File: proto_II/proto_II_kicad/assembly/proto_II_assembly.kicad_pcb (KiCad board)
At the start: 2 copper layers, 100 x 97 mm, 109 parts, among them J101 BOOT_CFG, J102 SNSR_I2C, J103 SNSR_PWR, J104 Vin, J105 RS485_A, J106 RS485_B, J107 ISO_GND, J108 Vin-5V, J109 SWD_DBG, J301 SIG_BYPASS, J302 PWR_BYPASS, SW101 RST, SW102 MODBUS_ADDR, SW103 USR_BTN, U101 STM32F103C8Tx, U201 TPS54331, U202 XC6206P332MR, U301 ADUM5241, U302 EL357N-G, U303 EL357N-G, U304 ST485EBDR, Y101 HSE, Y102 LSE

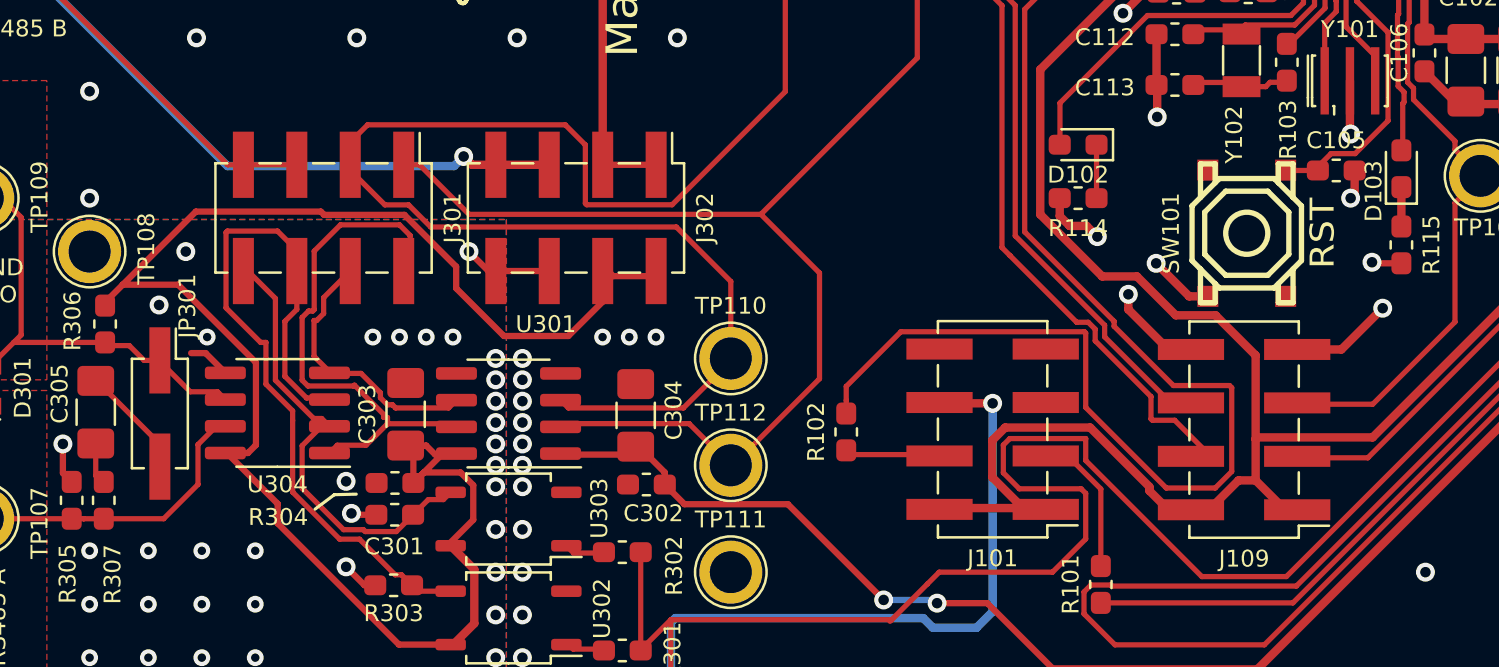
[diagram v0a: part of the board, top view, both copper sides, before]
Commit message: proto II: add more pin designators to silkscreen
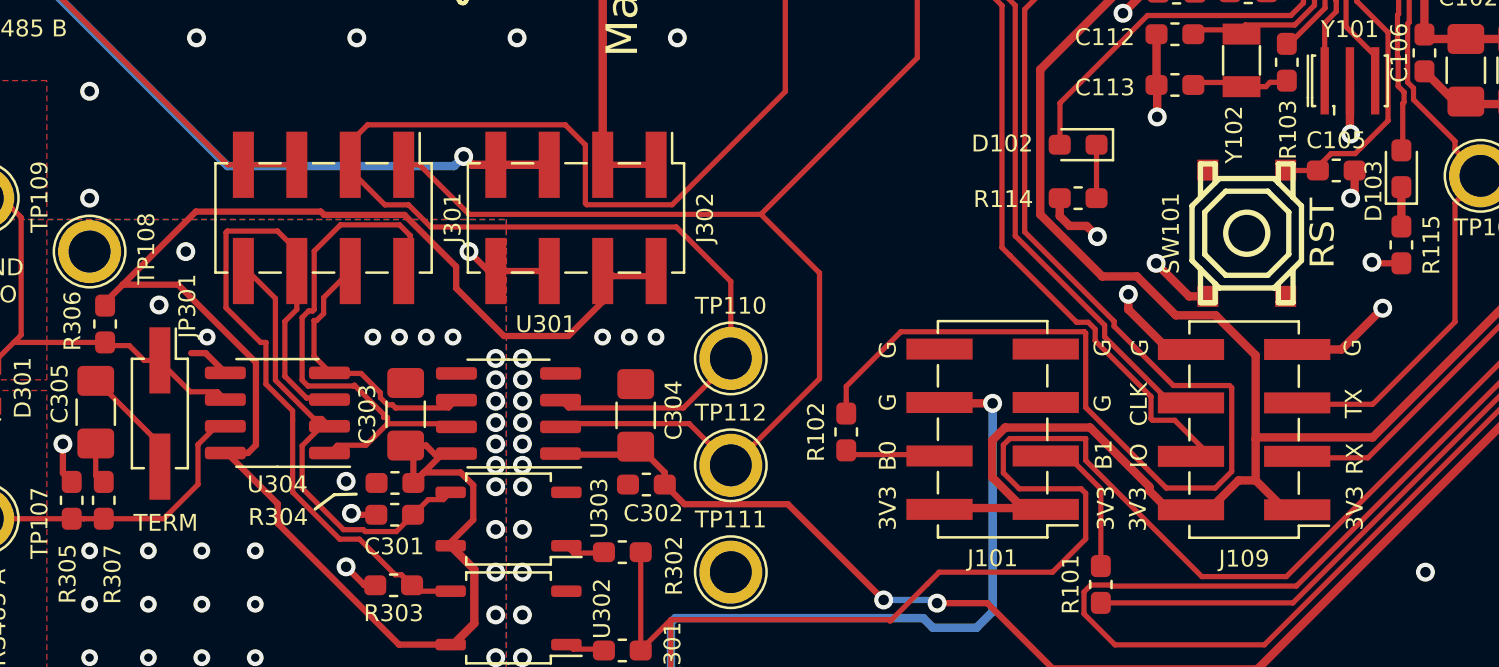
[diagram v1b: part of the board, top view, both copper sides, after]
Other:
- board text added: "3V3"
- board text added: "B0"
- board text added: "B1"
- board text added: "CLK"
- board text added: "G"
- board text added: "IO"
- board text added: "RX"
- board text added: "TERM"
- board text added: "TX"
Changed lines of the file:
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@@
   (general
     (thickness 1.6)
-    (drawings 589)
+    (drawings 606)
     (tracks 1098)
     (zones 0)
@@
   )
   (setup
-    (last_trace_width 0.4)
+    (last_trace_width 0.25)
     (user_trace_width 0.4)
     (trace_clearance 0.2)
@@
     (add_net "Net-(R301-Pad1)")
     (add_net "Net-(R302-Pad1)")
-    (add_net "Net-(U101-Pad10)")
-    (add_net "Net-(U101-Pad16)")
-    (add_net "Net-(U101-Pad18)")
-    (add_net "Net-(U101-Pad19)")
-    (add_net "Net-(U101-Pad21)")
-    (add_net "Net-(U101-Pad22)")
-    (add_net "Net-(U101-Pad25)")
-    (add_net "Net-(U101-Pad26)")
-    (add_net "Net-(U101-Pad27)")
-    (add_net "Net-(U101-Pad28)")
-    (add_net "Net-(U101-Pad45)")
-    (add_net "Net-(U101-Pad46)")
   )
   (net_class PWR ""
@@
     (tags "resistor handsolder")
     (attr smd)
-    (fp_text reference R114 (at 0 -1.43) (layer F.SilkS)
+    (fp_text reference R114 (at 3.556 -0.0508) (layer F.SilkS)
       (effects (font (size 0.8 0.8) (thickness 0.15)))
     )
@@
     (tags "diode handsolder")
     (attr smd)
-    (fp_text reference D102 (at 0 -1.43) (layer F.SilkS)
+    (fp_text reference D102 (at 3.6068 0.0508) (layer F.SilkS)
       (effects (font (size 0.8 0.8) (thickness 0.15)))
     )
@@
     )
   )
+  (gr_text IO (at 105.7656 111.3028 90) (layer F.SilkS)
+    (effects (font (size 0.8 0.8) (thickness 0.15)))
+  )
+  (gr_text CLK (at 105.7656 108.8644 90) (layer F.SilkS)
+    (effects (font (size 0.8 0.8) (thickness 0.15)))
+  )
+  (gr_text 3V3 (at 105.7148 113.8428 90) (layer F.SilkS)
+    (effects (font (size 0.8 0.8) (thickness 0.15)))
+  )
+  (gr_text 3V3 (at 116.0272 113.792 90) (layer F.SilkS)
+    (effects (font (size 0.8 0.8) (thickness 0.15)))
+  )
+  (gr_text 3V3 (at 104.1908 113.792 90) (layer F.SilkS)
+    (effects (font (size 0.8 0.8) (thickness 0.15)))
+  )
+  (gr_text RX (at 116.0272 111.4552 90) (layer F.SilkS)
+    (effects (font (size 0.8 0.8) (thickness 0.15)))
+  )
+  (gr_text TX (at 115.9764 108.8136 90) (layer F.SilkS)
+    (effects (font (size 0.8 0.8) (thickness 0.15)))
+  )
+  (gr_text G (at 115.9256 106.172 90) (layer F.SilkS)
+    (effects (font (size 0.8 0.8) (thickness 0.15)))
+  )
+  (gr_text G (at 105.8164 106.172 90) (layer F.SilkS)
+    (effects (font (size 0.8 0.8) (thickness 0.15)))
+  )
+  (gr_text G (at 104.0384 106.172 90) (layer F.SilkS)
+    (effects (font (size 0.8 0.8) (thickness 0.15)))
+  )
+  (gr_text G (at 104.0384 108.8136 90) (layer F.SilkS)
+    (effects (font (size 0.8 0.8) (thickness 0.15)))
+  )
+  (gr_text B1 (at 104.0892 111.252 90) (layer F.SilkS)
+    (effects (font (size 0.8 0.8) (thickness 0.15)))
+  )
+  (gr_text G (at 93.8276 106.2736 90) (layer F.SilkS)
+    (effects (font (size 0.8 0.8) (thickness 0.15)))
+  )
+  (gr_text G (at 93.8276 108.7628 90) (layer F.SilkS)
+    (effects (font (size 0.8 0.8) (thickness 0.15)))
+  )
+  (gr_text B0 (at 93.8276 111.3028 90) (layer F.SilkS)
+    (effects (font (size 0.8 0.8) (thickness 0.15)))
+  )
+  (gr_text 3V3 (at 93.8276 113.792 90) (layer F.SilkS)
+    (effects (font (size 0.8 0.8) (thickness 0.15)))
+  )
+  (gr_text TERM (at 59.5 114.5) (layer F.SilkS)
+    (effects (font (size 0.8 0.8) (thickness 0.15)))
+  )
   (gr_text "Proto II, rev0\n" (at 87 82 90) (layer F.SilkS)
     (effects (font (size 1.5 1.5) (thickness 0.3)))
@@
   (segment (start 121.714165 55.267767) (end 124.35607 55.267767) (width 0.4) (layer F.Cu) (net 2))
   (segment (start 112.826799 46.380401) (end 115.531999 49.085601) (width 0.4) (layer F.Cu) (net 2))
+  (segment (start 110.5408 60.9092) (end 110.5916 60.96) (width 0.4) (layer F.Cu) (net 2))
+  (segment (start 113.105469 60.730669) (end 113.1316 60.7568) (width 0.4) (layer F.Cu) (net 2))
+  (segment (start 113.336316 60.730669) (end 113.259331 60.730669) (width 0.4) (layer F.Cu) (net 2))
+  (segment (start 113.259331 60.730669) (end 113.336262 60.8076) (width 0.4) (layer F.Cu) (net 2))
+  (segment (start 121.960083 63.039917) (end 121.460083 63.039917) (width 0.4) (layer F.Cu) (net 2))
+  (segment (start 123.5 61.5) (end 121.960083 63.039917) (width 0.4) (layer F.Cu) (net 2))
+  (segment (start 121.460083 63.039917) (end 121.866317 63.039917) (width 0.4) (layer F.Cu) (net 2))
+  (segment (start 107.730669 60.730669) (end 108 61) (width 0.4) (layer F.Cu) (net 2))
+  (segment (start 108 61) (end 123.5 61) (width 0.4) (layer F.Cu) (net 2))
+  (segment (start 105.176864 63.039917) (end 121.460083 63.039917) (width 0.4) (layer F.Cu) (net 2))
+  (segment (start 123.5 61) (end 123.5 61.5) (width 0.4) (layer F.Cu) (net 2))
+  (segment (start 105.716316 60.730669) (end 107.730669 60.730669) (width 0.4) (layer F.Cu) (net 2))
+  (segment (start 121.460083 62.854436) (end 121.460083 63.039917) (width 0.4) (layer F.Cu) (net 2))
+  (segment (start 120.956316 62.350669) (end 121.460083 62.854436) (width 0.4) (layer F.Cu) (net 2))
+  (segment (start 120.956316 60.730669) (end 120.956316 62.350669) (width 0.4) (layer F.Cu) (net 2))
+  (segment (start 104.555458 60.931527) (end 103.068473 60.931527) (width 0.4) (layer F.Cu) (net 2))
+  (segment (start 105.716316 60.730669) (end 104.756316 60.730669) (width 0.4) (layer F.Cu) (net 2))
+  (segment (start 104.756316 60.730669) (end 104.555458 60.931527) (width 0.4) (layer F.Cu) (net 2))
+  (segment (start 100.560813 58.423866) (end 103.068473 60.931527) (width 0.4) (layer F.Cu) (net 2))
+  (segment (start 103.068473 60.931527) (end 105.176864 63.039917) (width 0.4) (layer F.Cu) (net 2))
   (segment (start 114.265908 97.744551) (end 112.794051 97.744551) (width 0.25) (layer F.Cu) (net 3) (status 30))
   (segment (start 112.794051 97.744551) (end 112.7125 97.663) (width 0.25) (layer F.Cu) (net 3) (status 30))
@@
   (segment (start 53.2135 71.062) (end 51.377 71.062) (width 0.4) (layer F.Cu) (net 49))
   (segment (start 51.377 71.062) (end 51.308 70.993) (width 0.4) (layer F.Cu) (net 49))
-  (segment (start 110.5408 60.9092) (end 110.5916 60.96) (width 0.4) (layer F.Cu) (net 2))
-  (segment (start 113.105469 60.730669) (end 113.1316 60.7568) (width 0.4) (layer F.Cu) (net 2))
-  (segment (start 113.336316 60.730669) (end 113.259331 60.730669) (width 0.4) (layer F.Cu) (net 2))
-  (segment (start 113.259331 60.730669) (end 113.336262 60.8076) (width 0.4) (layer F.Cu) (net 2))
-  (segment (start 121.960083 63.039917) (end 121.460083 63.039917) (width 0.4) (layer F.Cu) (net 2))
-  (segment (start 123.5 61.5) (end 121.960083 63.039917) (width 0.4) (layer F.Cu) (net 2))
-  (segment (start 121.460083 63.039917) (end 121.866317 63.039917) (width 0.4) (layer F.Cu) (net 2))
-  (segment (start 107.730669 60.730669) (end 108 61) (width 0.4) (layer F.Cu) (net 2))
-  (segment (start 108 61) (end 123.5 61) (width 0.4) (layer F.Cu) (net 2))
-  (segment (start 105.176864 63.039917) (end 121.460083 63.039917) (width 0.4) (layer F.Cu) (net 2))
-  (segment (start 123.5 61) (end 123.5 61.5) (width 0.4) (layer F.Cu) (net 2))
-  (segment (start 105.716316 60.730669) (end 107.730669 60.730669) (width 0.4) (layer F.Cu) (net 2))
-  (segment (start 121.460083 62.854436) (end 121.460083 63.039917) (width 0.4) (layer F.Cu) (net 2))
-  (segment (start 120.956316 62.350669) (end 121.460083 62.854436) (width 0.4) (layer F.Cu) (net 2))
-  (segment (start 120.956316 60.730669) (end 120.956316 62.350669) (width 0.4) (layer F.Cu) (net 2))
-  (segment (start 104.555458 60.931527) (end 103.068473 60.931527) (width 0.4) (layer F.Cu) (net 2))
-  (segment (start 105.716316 60.730669) (end 104.756316 60.730669) (width 0.4) (layer F.Cu) (net 2))
-  (segment (start 104.756316 60.730669) (end 104.555458 60.931527) (width 0.4) (layer F.Cu) (net 2))
-  (segment (start 100.560813 58.423866) (end 103.068473 60.931527) (width 0.4) (layer F.Cu) (net 2))
-  (segment (start 103.068473 60.931527) (end 105.176864 63.039917) (width 0.4) (layer F.Cu) (net 2))
   (segment (start 56.4745 71.062) (end 56.7975 70.739) (width 0.4) (layer F.Cu) (net 50))
   (segment (start 55.4995 71.062) (end 56.4745 71.062) (width 0.4) (layer F.Cu) (net 50))

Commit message: tmp: making rev1 started
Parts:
- removed C301, C302: 100n, Capacitor_SMD:C_0603_1608Metric_Pad1.05x0.95mm_HandSolder
- removed C303, C304: 1u, Capacitor_SMD:C_1206_3216Metric_Pad1.42x1.75mm_HandSolder
- removed C305: 10n, Capacitor_SMD:C_1206_3216Metric_Pad1.42x1.75mm_HandSolder
- removed D104: DI_LED, Diode_SMD:D_0603_1608Metric_Pad1.05x0.95mm_HandSolder
- removed D105: RO_LED, Diode_SMD:D_0603_1608Metric_Pad1.05x0.95mm_HandSolder
- removed J105: RS485_A, Project:DG300-5.0-02P-12
- removed J106: RS485_B, Project:DG300-5.0-02P-12
- removed J108: Vin-5V, Project:DG300-5.0-02P-12
- removed J301: SIG_BYPASS, Connector_PinHeader_2.54mm:PinHeader_2x04_P2.54mm_Vertical_SMD
- removed J302: PWR_BYPASS, Connector_PinHeader_2.54mm:PinHeader_2x04_P2.54mm_Vertical_SMD
- removed R102, R112, R303, R304: 10K, Resistor_SMD:R_0603_1608Metric_Pad1.05x0.95mm_HandSolder
- removed R116, R117, R301, R302, R305, R306: 2K2, Resistor_SMD:R_0603_1608Metric_Pad1.05x0.95mm_HandSolder
- removed the REF** at (132.6, 33.0)
- removed SW103: USR_BTN, Project:Tactile_Switch_5x5mm
- removed TP104: U2_RX, TestPoint:TestPoint_Plated_Hole_D2.0mm
- removed TP112: U1_TX, TestPoint:TestPoint_Plated_Hole_D2.0mm
- removed U301: ADUM5241, Package_SO:SOIC-8_3.9x4.9mm_P1.27mm
- removed U302, U303: EL357N-G, Package_SO:SOP-4_3.8x4.1mm_P2.54mm
- removed U304: ST485EBDR, Package_SO:SOIC-8_3.9x4.9mm_P1.27mm
- added C25: 100n, Capacitor_SMD:C_0603_1608Metric_Pad1.05x0.95mm_HandSolder, F.Cu at (174.5, 117.2)
- added C26: 10u, Capacitor_SMD:CP_Elec_6.3x5.7, F.Cu at (190.5, 105.6)
- added C27: 10n, Capacitor_SMD:C_1206_3216Metric_Pad1.42x1.75mm_HandSolder, F.Cu at (198.7, 103.2)
- added C28: 100n, Capacitor_SMD:C_0603_1608Metric_Pad1.05x0.95mm_HandSolder, F.Cu at (178.9, 117.2)
- added C29: 100n, Capacitor_SMD:C_0603_1608Metric_Pad1.05x0.95mm_HandSolder, F.Cu at (197.9, 109.4)
- added C30: 10n, Capacitor_SMD:C_1206_3216Metric_Pad1.42x1.75mm_HandSolder, F.Cu at (56.2, 109.2)
- added C31: 10u, Capacitor_SMD:CP_Elec_6.3x5.7, F.Cu at (190.5, 113.8)
- added C32: 100n, Capacitor_SMD:C_0603_1608Metric_Pad1.05x0.95mm_HandSolder, F.Cu at (197.9, 111.9)
- added C33: 10n, Capacitor_SMD:C_1206_3216Metric_Pad1.42x1.75mm_HandSolder, F.Cu at (198.7, 106.5)
- added D4: DI_LED, Diode_SMD:D_0603_1608Metric_Pad1.05x0.95mm_HandSolder, F.Cu at (90.7, 80.5)
- added D5: RO_LED, Diode_SMD:D_0603_1608Metric_Pad1.05x0.95mm_HandSolder, F.Cu at (93.0, 80.5)
- added J5: RS485_A, Project:DG300-5.0-02P-12, F.Cu at (44.0, 98.0)
- added J6: RS485_B, Project:DG300-5.0-02P-12, F.Cu at (44.0, 118.0)
- added R12: 10K, Resistor_SMD:R_0603_1608Metric_Pad1.05x0.95mm_HandSolder, F.Cu at (123.8, 88.7)
- added R16: 2K2, Resistor_SMD:R_0603_1608Metric_Pad1.05x0.95mm_HandSolder, F.Cu at (90.7, 77.2)
- added R17: 2K2, Resistor_SMD:R_0603_1608Metric_Pad1.05x0.95mm_HandSolder, F.Cu at (93.0, 77.2)
- added R2: 10K, Resistor_SMD:R_0603_1608Metric_Pad1.05x0.95mm_HandSolder, F.Cu at (91.8, 110.2)
- added SW3: USR_BTN, Project:Tactile_Switch_5x5mm, F.Cu at (129.5, 88.9)
- added TP12: U1_TX, TestPoint:TestPoint_Pad_D1.0mm, F.Cu at (96.5, 88.9)
- added TP16: U1_B0, TestPoint:TestPoint_Pad_D1.0mm, F.Cu at (91.4, 106.7)
- added TP17: G_U1, TestPoint:TestPoint_Pad_D1.0mm, F.Cu at (91.4, 104.1)
- added TP18: U1_B1, TestPoint:TestPoint_Pad_D1.0mm, F.Cu at (101.6, 119.4)
- added TP19: U1_B0, TestPoint:TestPoint_Pad_D1.0mm, F.Cu at (96.5, 83.8)
- added TP20: G_U1, TestPoint:TestPoint_Pad_D1.0mm, F.Cu at (104.1, 83.8)
- added TP21: U1_B1, TestPoint:TestPoint_Pad_D1.0mm, F.Cu at (101.6, 83.8)
- added TP22: DE_RE, TestPoint:TestPoint_Pad_D1.0mm, F.Cu at (88.9, 119.4)
- added TP4: U2_RX, TestPoint:TestPoint_Pad_D1.0mm, F.Cu at (86.4, 99.1)
- added U4: ADM2587E, Package_SO:SOIC-20W_7.5x12.8mm_P1.27mm, F.Cu at (178.8, 108.7)
- JP1: renamed from JP301; footprint Connector_PinHeader_2.54mm:PinHeader_2x01_P2.54mm_Vertical_SMD -> Button_Switch_SMD:SW_DIP_SPSTx01_Slide_9.78x4.72mm_W8.61mm_P2.54mm
- TP1: renamed from TP101; footprint TestPoint:TestPoint_Plated_Hole_D2.0mm -> TestPoint:TestPoint_Pad_D1.0mm
- TP10: renamed from TP110; footprint TestPoint:TestPoint_Plated_Hole_D2.0mm -> TestPoint:TestPoint_Pad_D1.0mm
- TP11: renamed from TP111; footprint TestPoint:TestPoint_Plated_Hole_D2.0mm -> TestPoint:TestPoint_Pad_D1.0mm
- TP13: renamed from TP113; footprint TestPoint:TestPoint_Plated_Hole_D2.0mm -> TestPoint:TestPoint_Pad_D1.0mm
- TP14: renamed from TP114; footprint TestPoint:TestPoint_Plated_Hole_D2.0mm -> TestPoint:TestPoint_Pad_D1.0mm
- TP15: renamed from TP115; footprint TestPoint:TestPoint_Plated_Hole_D2.0mm -> TestPoint:TestPoint_Pad_D1.0mm
- TP2: renamed from TP102; footprint TestPoint:TestPoint_Plated_Hole_D2.0mm -> TestPoint:TestPoint_Pad_D1.0mm
- TP3: renamed from TP103; footprint TestPoint:TestPoint_Plated_Hole_D2.0mm -> TestPoint:TestPoint_Pad_D1.0mm
- TP5: renamed from TP105; footprint TestPoint:TestPoint_Plated_Hole_D2.0mm -> TestPoint:TestPoint_Pad_D1.0mm
- TP6: renamed from TP106; footprint TestPoint:TestPoint_Plated_Hole_D2.0mm -> TestPoint:TestPoint_Pad_D1.0mm
- TP7: renamed from TP107; footprint TestPoint:TestPoint_Plated_Hole_D2.0mm -> TestPoint:TestPoint_Pad_D1.0mm
- TP8: renamed from TP108; footprint TestPoint:TestPoint_Plated_Hole_D2.0mm -> TestPoint:TestPoint_Pad_D1.0mm
- TP9: renamed from TP109; footprint TestPoint:TestPoint_Plated_Hole_D2.0mm -> TestPoint:TestPoint_Pad_D1.0mm
- moved TP5 43.8 mm to (86.4, 101.6)
- moved TP6 35.7 mm to (86.4, 96.5)
- moved TP11 25.0 mm to (96.5, 94.0)
- moved TP10 18.5 mm to (91.4, 88.9)
- moved TP7 17.8 mm to (50.8, 96.5)
- moved TP9 17.8 mm to (50.8, 116.8)
- moved TP8 14.2 mm to (62.2, 114.3)
- moved JP1 7.29 mm to (60.5, 102.1), turned to 180 degrees
- renumbered C101 to C1, C110 to C10, C111 to C11, C112 to C12, C113 to C13, C201 to C14, C202 to C15, C203 to C16, C204 to C17, C205 to C18, C206 to C19, C102 to C2, C207 to C20, C208 to C21, C209 to C22, C210 to C23, C211 to C24, C103 to C3, C104 to C4, C105 to C5, C106 to C6, C107 to C7, C108 to C8, C109 to C9, D101 to D1, D102 to D2, D103 to D3, D201 to D6, D301 to D7, J101 to J1, J102 to J2, J103 to J3, J104 to J4, J107 to J7, J109 to J8, L201 to L1, R101 to R1, R110 to R10, R111 to R11, R113 to R13, R114 to R14, R115 to R15, R201 to R18, R202 to R19, R203 to R20, R204 to R21, R205 to R22, R307 to R23, R103 to R3, R104 to R4, R105 to R5, R106 to R6, R107 to R7, R108 to R8, R109 to R9, SW101 to SW1, SW102 to SW2, U101 to U1, U201 to U2, U202 to U3, Y101 to Y1, Y102 to Y2
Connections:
- J8 pad 3: /UART2_RX -> /UART1_RX
- J8 pad 5: /UART2_TX -> /UART1_TX
- TP6 pad 1: /UART2_TX -> /UART3_TX
- U1 pad 12: /UART2_TX -> (no net)
- U1 pad 13: /UART2_RX -> (no net)
- U1 pad 21: (no net) -> /UART3_TX
- U1 pad 22: (no net) -> /UART3_RX
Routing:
- net +5V: track 344.2 -> 143.6 mm, vias 2 -> 0
- net /UART3_TX: track 0.00 -> 182.2 mm, vias 0 -> 6
- net /UART3_RX: track 0.00 -> 166.4 mm, vias 0 -> 8
- net GND: track 248.0 -> 116.3 mm, vias 106 -> 148
- net /MODBUS_A7: track 248.6 -> 136.2 mm, vias 2 -> 4
- net /DE~RE: track 211.2 -> 101.7 mm
- net /UART2_RX: track 43.5 -> 0.00 mm
- net +5VD: track 80.4 -> 45.6 mm
- net /UART2_TX: track 27.7 -> 0.00 mm
- net /rs485/DE_XMTR: track 35.5 -> 14.7 mm
- net /rs485/RO_XMTR: track 26.3 -> 6.80 mm
- net /UART1_TX: track 136.1 -> 118.8 mm, vias 0 -> 4
- net +3V3: track 363.4 -> 353.1 mm
- net /RS485_B: track 20.9 -> 30.1 mm
- net /rs485/RE_XMTR: track 21.3 -> 12.2 mm
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- added copper zone on F.Cu, net +3V3
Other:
- net class PWR_THICK added: clearance 0.2, trace_width 0.4, via_dia 0.9, via_drill 0.5
- board text added: "Proto II, rev1"
- board text added: "RS485 Termination"
- board text removed: "Proto II, rev0"
- board text removed: "TERM"
- board text removed: "Vin 5V"

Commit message: tmp: more work
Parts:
- L1: value 22u -> 47u; footprint Project:CDRH74 -> Project:SWRB1205S
- moved L1 127.2 mm to (177.8, 132.0), turned to 270 degrees
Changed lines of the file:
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@@
     (uvia_drill 0.1)
   )
+  (module Project:SWRB1205S (layer F.Cu)
+    (at 177.77206 131.96952 270)
+    (descr "Sunlord Wire Wound SMD Power Inductors – SWRB-S Series")
+    (tags Sunlord,SWRB1205S,Inductor,choke,coil)
+    (attr smd)
+    (fp_text reference L1 (at 0.5 -7.5 90) (layer F.SilkS)
+      (effects (font (size 1 1) (thickness 0.15)))
+    )
+    (fp_text value 47u (at 0 -9 90) (layer F.Fab)
+      (effects (font (size 1 1) (thickness 0.15)))
+    )
+    (fp_line (start -6.5 6.5) (end -6.5 -6.5) (layer F.SilkS) (width 0.15))
+    (fp_line (start 6.5 6.5) (end -6.5 6.5) (layer F.SilkS) (width 0.15))
+    (fp_line (start 6.5 -6.5) (end 6.5 6.5) (layer F.SilkS) (width 0.15))
+    (fp_line (start -6.5 -6.5) (end 6.5 -6.5) (layer F.SilkS) (width 0.15))
+    (fp_line (start -6.5 -6.5) (end 0 -6.5) (layer F.CrtYd) (width 0.02))
+    (fp_line (start -6.5 0) (end -6.5 -6.5) (layer F.CrtYd) (width 0.02))
+    (fp_line (start -6.5 6.5) (end -6.5 0) (layer F.CrtYd) (width 0.02))
+    (fp_line (start 0 6.5) (end -6.5 6.5) (layer F.CrtYd) (width 0.02))
+    (fp_line (start 6.5 6.5) (end 0 6.5) (layer F.CrtYd) (width 0.02))
+    (fp_line (start 6.5 0) (end 6.5 6.5) (layer F.CrtYd) (width 0.02))
+    (fp_line (start 6.5 -6.5) (end 6.5 0) (layer F.CrtYd) (width 0.02))
+    (fp_line (start 0 -6.5) (end 6.5 -6.5) (layer F.CrtYd) (width 0.02))
+    (pad 2 smd rect (at 5 0 270) (size 2.9 5.4) (layers F.Cu F.Paste F.Mask)
+      (net 6 +5V))
+    (pad 1 smd rect (at -5 0 270) (size 2.9 5.4) (layers F.Cu F.Paste F.Mask)
+      (net 5 /power/PH))
+    (model ${KIPRJMOD}/../common/3d/CDRN74.stp
+      (at (xyz 0 0 0))
+      (scale (xyz 1 1 1))
+      (rotate (xyz -90 0 0))
+    )
+  )
   (module Package_SO:SOIC-20W_7.5x12.8mm_P1.27mm (layer F.Cu)
     (at 178.79832 108.72496)
@@
     )
   )
-  (module Project:CDRH74 (layer F.Cu)
-    (at 70.7395 63.1515 180)
-    (descr "Sumidia SMD Power Inductor ")
-    (tags Sumidia,CDRH74,Inductor,choke,coil)
-    (attr smd)
-    (fp_text reference L1 (at -2.794 -5.08) (layer F.SilkS)
-      (effects (font (size 0.8 0.8) (thickness 0.15)))
-    )
-    (fp_text value 22u (at 0 -6.5) (layer F.Fab)
-      (effects (font (size 1 1) (thickness 0.15)))
-    )
-    (fp_line (start 3.7 -4.2) (end 3.7 4.2) (layer F.SilkS) (width 0.15))
-    (fp_line (start -3.7 4.2) (end -3.7 -4.2) (layer F.SilkS) (width 0.15))
-    (fp_line (start -3.7 -4.2) (end 3.7 -4.2) (layer F.SilkS) (width 0.15))
-    (fp_line (start 3.7 4.2) (end -3.7 4.2) (layer F.SilkS) (width 0.15))
-    (fp_line (start -3.7 -4.2) (end 3.7 -4.2) (layer F.CrtYd) (width 0.02))
-    (fp_line (start 3.7 -4.2) (end 3.7 4.2) (layer F.CrtYd) (width 0.02))
-    (fp_line (start 3.7 4.2) (end -3.7 4.2) (layer F.CrtYd) (width 0.02))
-    (fp_line (start -3.7 4.2) (end -3.7 -4.2) (layer F.CrtYd) (width 0.02))
-    (pad 1 smd rect (at 0 -3.2 180) (size 2.2 1.6) (layers F.Cu F.Paste F.Mask)
-      (net 5 /power/PH))
-    (pad 2 smd rect (at 0 3.2 180) (size 2.2 1.6) (layers F.Cu F.Paste F.Mask)
-      (net 6 +5V))
-    (model ${KIPRJMOD}/../common/3d/CDRN74.stp
-      (at (xyz 0 0 0))
-      (scale (xyz 1 1 1))
-      (rotate (xyz -90 0 0))
-    )
-  )
